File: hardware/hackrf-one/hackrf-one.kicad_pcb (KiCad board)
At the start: 4 copper layers, 120 x 75 mm, 432 parts, among them J1 USB-MICRO-B, J10 GND_CLIP, J2 RF-SHIELD-FRAME, J3 RF-SHIELD-COVER, J4 MOUNTING_HOLE, J5 MOUNTING_HOLE, J6 MOUNTING_HOLE, J7 MOUNTING_HOLE, J8 MOUNTING_HOLE, J9 MOUNTING_HOLE, P1 1V8, P13 GPO1, P14 XCVR_CLKOUT, P15 INTR, P16 CLKIN, P17 GPO6, P18 OEB, P19 GPO3, P2 CLKOUT, P20 GPIO, P21 REF_IN, P22 I2S, P23 DBGEN, P24 TRST, P25 LPC_ISP, P26 LPC_JTAG, P27 MIXER_SDATA, P28 SD, P29 CPLD_JTAG, P3 GND, P30 BANK2_AUX, P31 MIXER_SCLK, P32 MIXER_ENX, P33 MIXER_RESETX, P34 MIX_BYPASS, P35 !MIX_BYPASS, P36 VAA, P37 SCL, P38 SDA, P39 SSP1_SCK, P4 ANTENNA, P40 SSP1_MOSI, P41 SSP1_MISO, P42 TX, P43 RX, P44 HP, P45 LP, P46 TX_MIX_BP, P47 RX_MIX_BP, P48 TX_AMP, P49 RX_AMP, P5 LEDS, P50 AMP_BYPASS, P51 !TX_AMP_PWR, P52 !RX_AMP_PWR, P53 CS_XCVR, P54 CS_AD, P55 TXENABLE, P56 RXENABLE, P57 XTAL2, P58 GCK1, P59 GCK2, P6 GPO4, P60 SGPIO_CLK, P61 DA0, P62 DA7, P63 DD0, P64 DD9, P65 DA4, P66 DD5, P67 RSSI, P68 SPIFI_CS, P69 VREGMODE, P7 GPO2, P70 EN_1V8, P71 ID, P72 GP_CLKIN, P73 P1_2, P74 P1_1, P75 GP_CLKIN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

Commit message: HackRF One: changed VBUS voltage divider to match GreatFET One
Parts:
- R62: value 0 -> 10k
- R65: value 10k -> 18k
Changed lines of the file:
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@@
       (effects (font (size 0.4064 0.4064) (thickness 0.1016)))
     )
-    (fp_text value 0 (at 0 0.0508) (layer F.SilkS) hide
+    (fp_text value 10k (at 0 0.0508) (layer F.SilkS) hide
       (effects (font (size 0.4064 0.4064) (thickness 0.1016)))
     )
@@
       (effects (font (size 0.4064 0.4064) (thickness 0.1016)))
     )
-    (fp_text value 10k (at 0 0.0508 180) (layer F.SilkS) hide
+    (fp_text value 18k (at 0 0.0508 180) (layer F.SilkS) hide
       (effects (font (size 0.4064 0.4064) (thickness 0.1016)))
     )

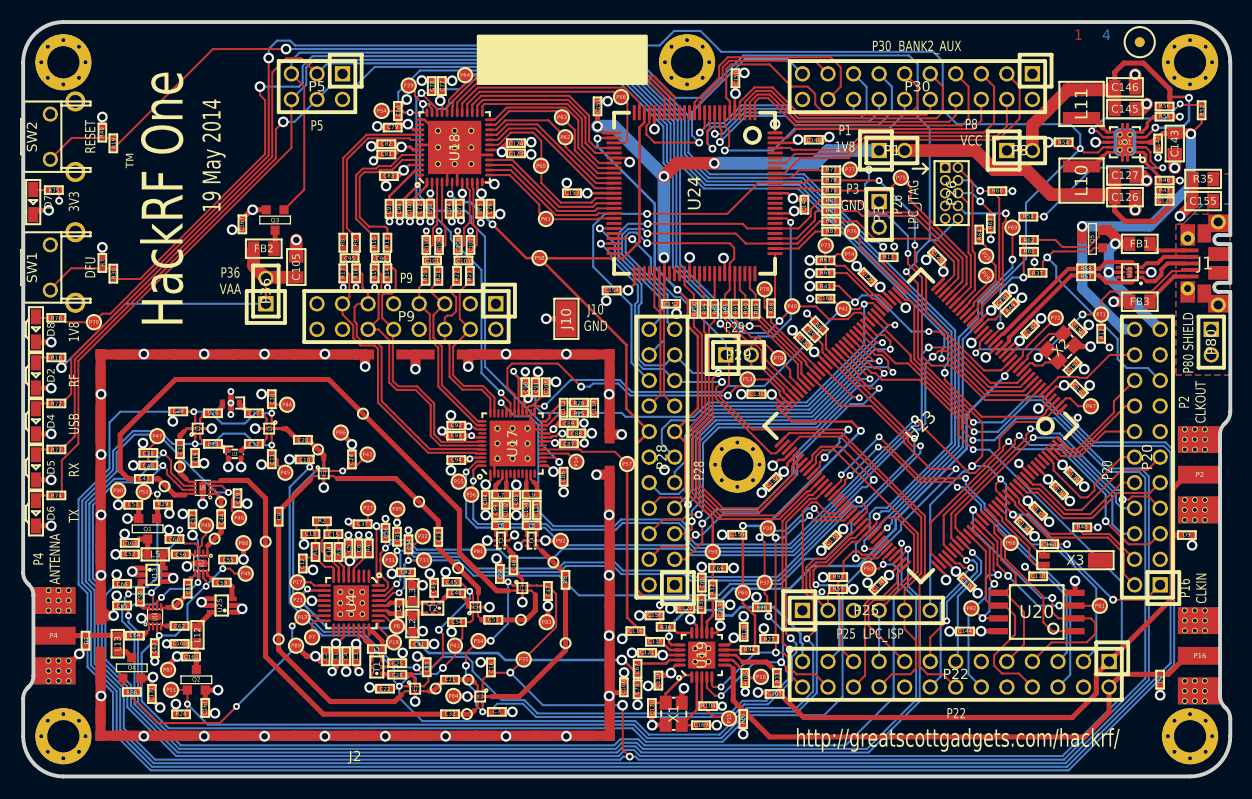
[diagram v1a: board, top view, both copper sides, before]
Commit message: HackRF One: updated layout to match recent changes to schematic
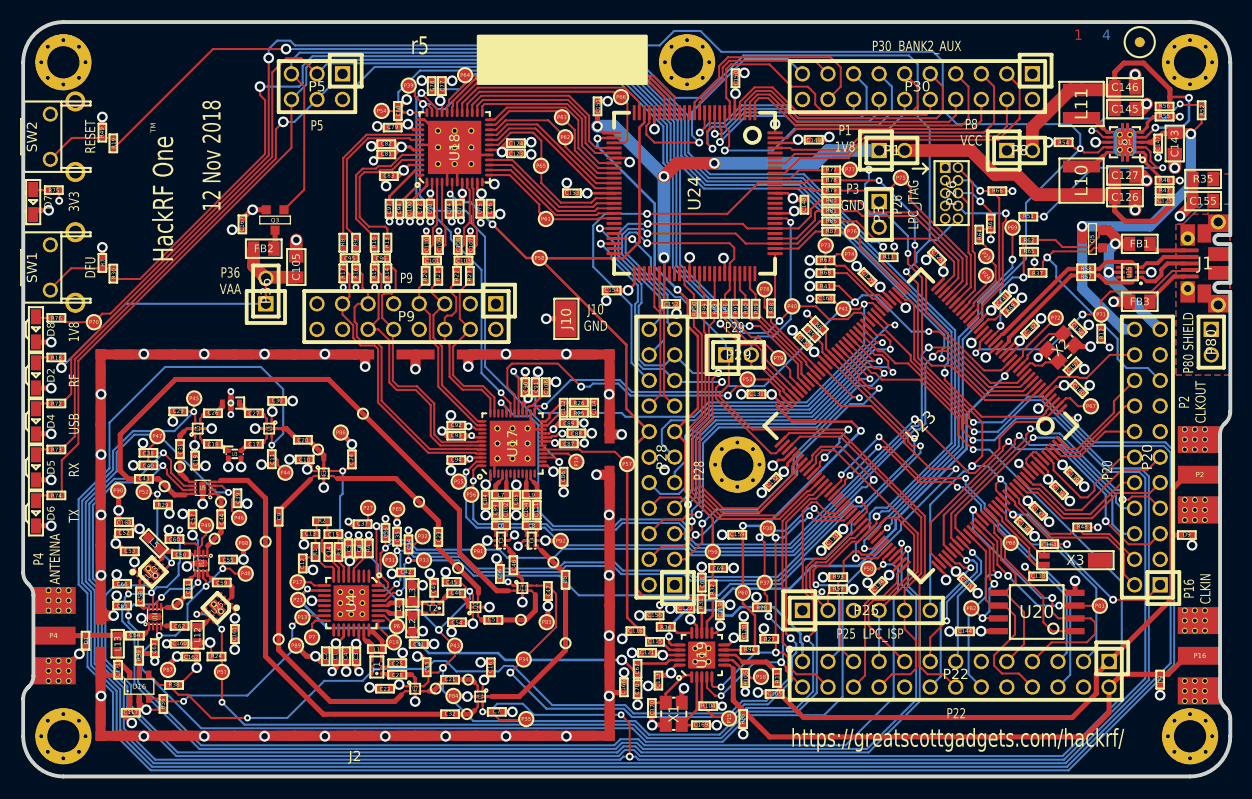
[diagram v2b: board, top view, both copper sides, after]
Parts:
- removed P42: TX, hackrf:GSG-TESTPOINT-50MIL
- removed Q1, Q2, Q4: MOSFET_P, gsg-modules:SOT23GDS
- added C117: 100nF, hackrf:GSG-0402, F.Cu at (70.7, 168.7)
- added R38: 10k, hackrf:GSG-0402, F.Cu at (75.0, 165.9)
- added R39: 0, hackrf:GSG-0402, F.Cu at (71.5, 163.0)
- added U16: AP2553W6-7, gsg-modules:SOT457, F.Cu at (71.5, 166.1)
- C10, C16, C19, C22, C30, C54, C56: value 33pF -> 10nF
- C169, C170: value DNP -> 1.8pF
- U1, U10, U11, U2, U5, U6, U7: value SKY13350 -> SKY13453
- U13: value MGA-81563 -> TRF37D73; footprint hackrf:GSG-SOT363 -> gsg-modules:WSON8
- U15: value LXES1TBCC2-004 -> TVS
- U25: value MGA-81563 -> TRF37A73; footprint hackrf:GSG-SOT363 -> gsg-modules:WSON8
- moved P45 11.7 mm to (77.0, 137.4)
- moved C161 7.91 mm to (81.0, 160.8)
- moved P44 6.76 mm to (86.1, 144.8)
- moved R24 6.74 mm to (79.2, 163.1)
- moved P35 5.93 mm to (110.0, 169.3)
- moved P51 5.36 mm to (79.8, 164.6)
- moved P34 4.85 mm to (109.8, 163.4)
- moved C53 4.63 mm to (70.6, 152.6)
- moved C171 4.13 mm to (69.4, 164.4)
- moved R36 3.36 mm to (73.9, 167.8), turned to 270 degrees
- moved C52 2.18 mm to (70.0, 150.8)
- moved C163 2.13 mm to (70.0, 149.7)
- moved L5 1.11 mm to (73.0, 151.8), turned to 315 degrees
- moved C30 0.56 mm to (85.2, 137.7), turned to 180 degrees
- moved U25 0.49 mm to (79.3, 158.2), turned to 225 degrees
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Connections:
- net /frontend/!ANT_BIAS renamed /frontend/ANT_BIAS_EN
- net Net-(C58-Pad1) renamed /frontend/RX_AMP_IN
- C10 pad 2: RX -> VAA
- C11 pad 2: LP -> HP
- C16 pad 1: !MIX_BYPASS -> GND
- C16 pad 2: GND -> VAA
- C160 pad 1: Net-(C160-Pad1) -> VAA
- C162 pad 2: Net-(C160-Pad1) -> VAA
- C163 pad 2: Net-(C163-Pad2) -> VAA
- C171 pad 1: VAA -> Net-(C171-Pad1)
- C19 pad 2: LP -> VAA
- C22 pad 2: RX -> VAA
- C24 pad 2: TX -> RX
- C29 pad 1: HP -> LP
- C30 pad 1: HP -> GND
- C30 pad 2: GND -> VAA
- C33 pad 1: TX -> RX
- C45 pad 2: TX -> RX
- C47 pad 2: !MIX_BYPASS -> MIX_BYPASS
- C52 pad 1: Net-(C163-Pad2) -> VAA
- C54 pad 1: RX -> GND
- C54 pad 2: GND -> VAA
- C56 pad 1: MIX_BYPASS -> GND
- C56 pad 2: GND -> VAA
- C7 pad 2: MIX_BYPASS -> !MIX_BYPASS
- L12 pad 1: Net-(C160-Pad1) -> VAA
- L13 pad 1: Net-(L13-Pad1) -> Net-(C171-Pad1)
- L5 pad 1: Net-(C163-Pad2) -> VAA
- R29 pad 1: VAA -> !RX_AMP_PWR
- R29 pad 2: !RX_AMP_PWR -> VAA
- R36 pad 2: VAA -> GND
- U1 pad 1: !MIX_BYPASS -> VAA
- U1 pad 5: MIX_BYPASS -> !MIX_BYPASS
- U10 pad 1: RX -> VAA
- U10 pad 5: TX -> RX
- U11 pad 1: MIX_BYPASS -> VAA
- U11 pad 5: !MIX_BYPASS -> MIX_BYPASS
- U13 pad 1: GND -> VAA
- U13 pad 2: GND -> Net-(C58-Pad2)
- U13 pad 3: Net-(C58-Pad2) -> Net-(U13-Pad3)
- U13 pad 4: GND -> Net-(U13-Pad4)
- U13 pad 5: GND -> !RX_AMP_PWR
- U13 pad 6: Net-(C50-Pad1) -> Net-(U13-Pad6)
- U2 pad 1: RX -> VAA
- U2 pad 5: TX -> RX
- U23 pad 136: Net-(U23-Pad136) -> VCC
- U23 pad 138: Net-(U23-Pad138) -> VCC
- U23 pad 139: Net-(U23-Pad139) -> VCC
- U23 pad 85: TX -> !ANT_BIAS_FAULT
- U25 pad 1: GND -> VAA
- U25 pad 2: GND -> Net-(C59-Pad2)
- U25 pad 3: Net-(C59-Pad2) -> Net-(U25-Pad3)
- U25 pad 4: GND -> Net-(U25-Pad4)
- U25 pad 5: GND -> !TX_AMP_PWR
- U25 pad 6: Net-(C62-Pad2) -> Net-(U25-Pad6)
- U5 pad 1: LP -> VAA
- U5 pad 5: HP -> LP
- U6 pad 1: HP -> VAA
- U6 pad 5: LP -> HP
- U7 pad 1: RX -> VAA
- U7 pad 5: TX -> RX
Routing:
- net TX: track 115.0 -> 0.00 mm, vias 5 -> 0
- net !ANT_BIAS_FAULT: track 0.00 -> 93.3 mm, vias 0 -> 2
- net VAA: track 92.7 -> 117.8 mm, vias 27 -> 36
- net LP: track 225.5 -> 214.3 mm, vias 3 -> 2
- net !MIX_BYPASS: track 237.4 -> 227.4 mm
- net MIX_BYPASS: track 74.6 -> 65.9 mm, vias 5 -> 2
- net RX: track 114.9 -> 106.9 mm, vias 4 -> 5
- net HP: track 202.5 -> 210.5 mm, vias 3 -> 2
- net VCC: track 183.7 -> 190.6 mm
- net /frontend/ANT_BIAS_EN: track 28.4 -> 22.5 mm
- net Net-(C163-Pad2): track 4.17 -> 0.00 mm
- net Net-(C160-Pad1): track 4.04 -> 0.00 mm
- net !TX_AMP_PWR: track 90.7 -> 94.6 mm, vias 2 -> 4
- net Net-(C171-Pad1): track 0.00 -> 3.00 mm
- net TX_AMP: track 143.2 -> 141.3 mm
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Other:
- board text added: "12 Nov 2018"
- board text added: "https://greatscottgadgets.com/hackrf/"
- board text added: "r5"
- board text removed: "19 May 2014"
- board text removed: "http://greatscottgadgets.com/hackrf/"

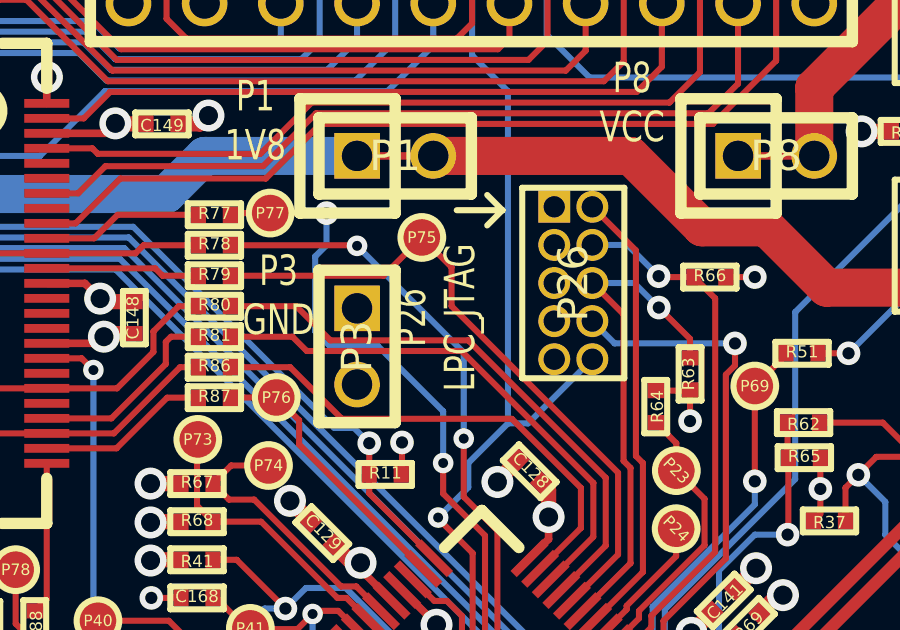
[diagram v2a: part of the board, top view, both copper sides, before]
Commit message: HackRF One: replaced various capacitors that are NRND
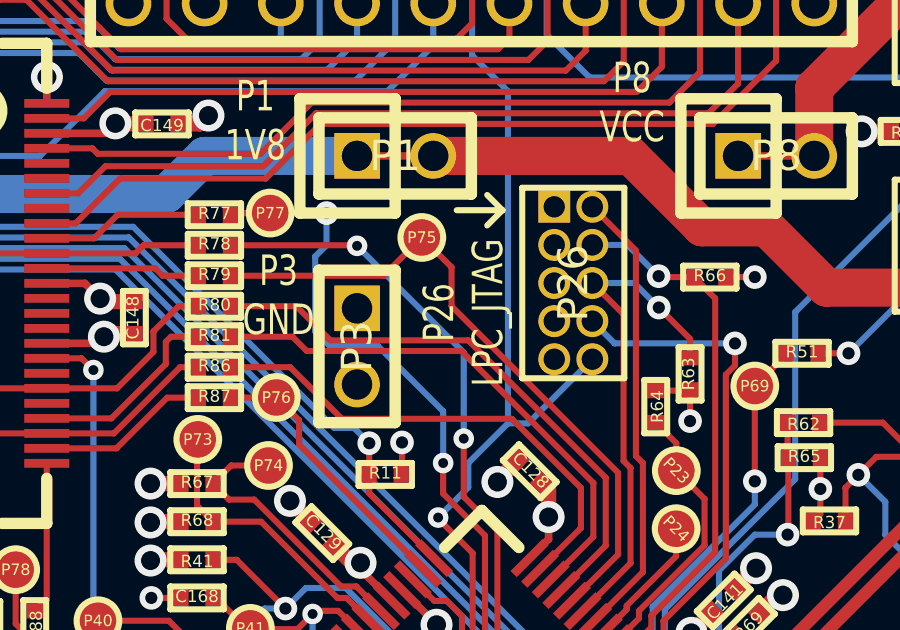
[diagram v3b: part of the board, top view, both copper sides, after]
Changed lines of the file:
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@@
     (effects (font (size 1.016 0.762) (thickness 0.1905)))
   )
-  (gr_text "P26\nLPC_JTAG" (at 147.7062 118.1548 90) (layer F.SilkS)
+  (gr_text "P26\nLPC_JTAG" (at 148.64 117.99 90) (layer F.SilkS)
     (effects (font (size 1.016 0.762) (thickness 0.1905)))
   )
